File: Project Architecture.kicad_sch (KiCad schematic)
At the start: 0 parts

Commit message: SCH[Power & Balance]: Inital Schamtic for two pages.
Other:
- removed sheet Section A - Title A
- removed sheet Section B - Title B
- added sheet Cell Sense & Balance (cell_sense_and_balance.kicad_sch)
- added sheet Connectors (connectors.kicad_sch)
- added sheet Daisy Chain (daisy_chain.kicad_sch)
- added sheet Mechanical (mechanical.kicad_sch)
- added sheet Power & Reference (power_and_reference.kicad_sch)
- added sheet Temperature Sense (temperature_sense.kicad_sch)
- note removed: "Page 5"

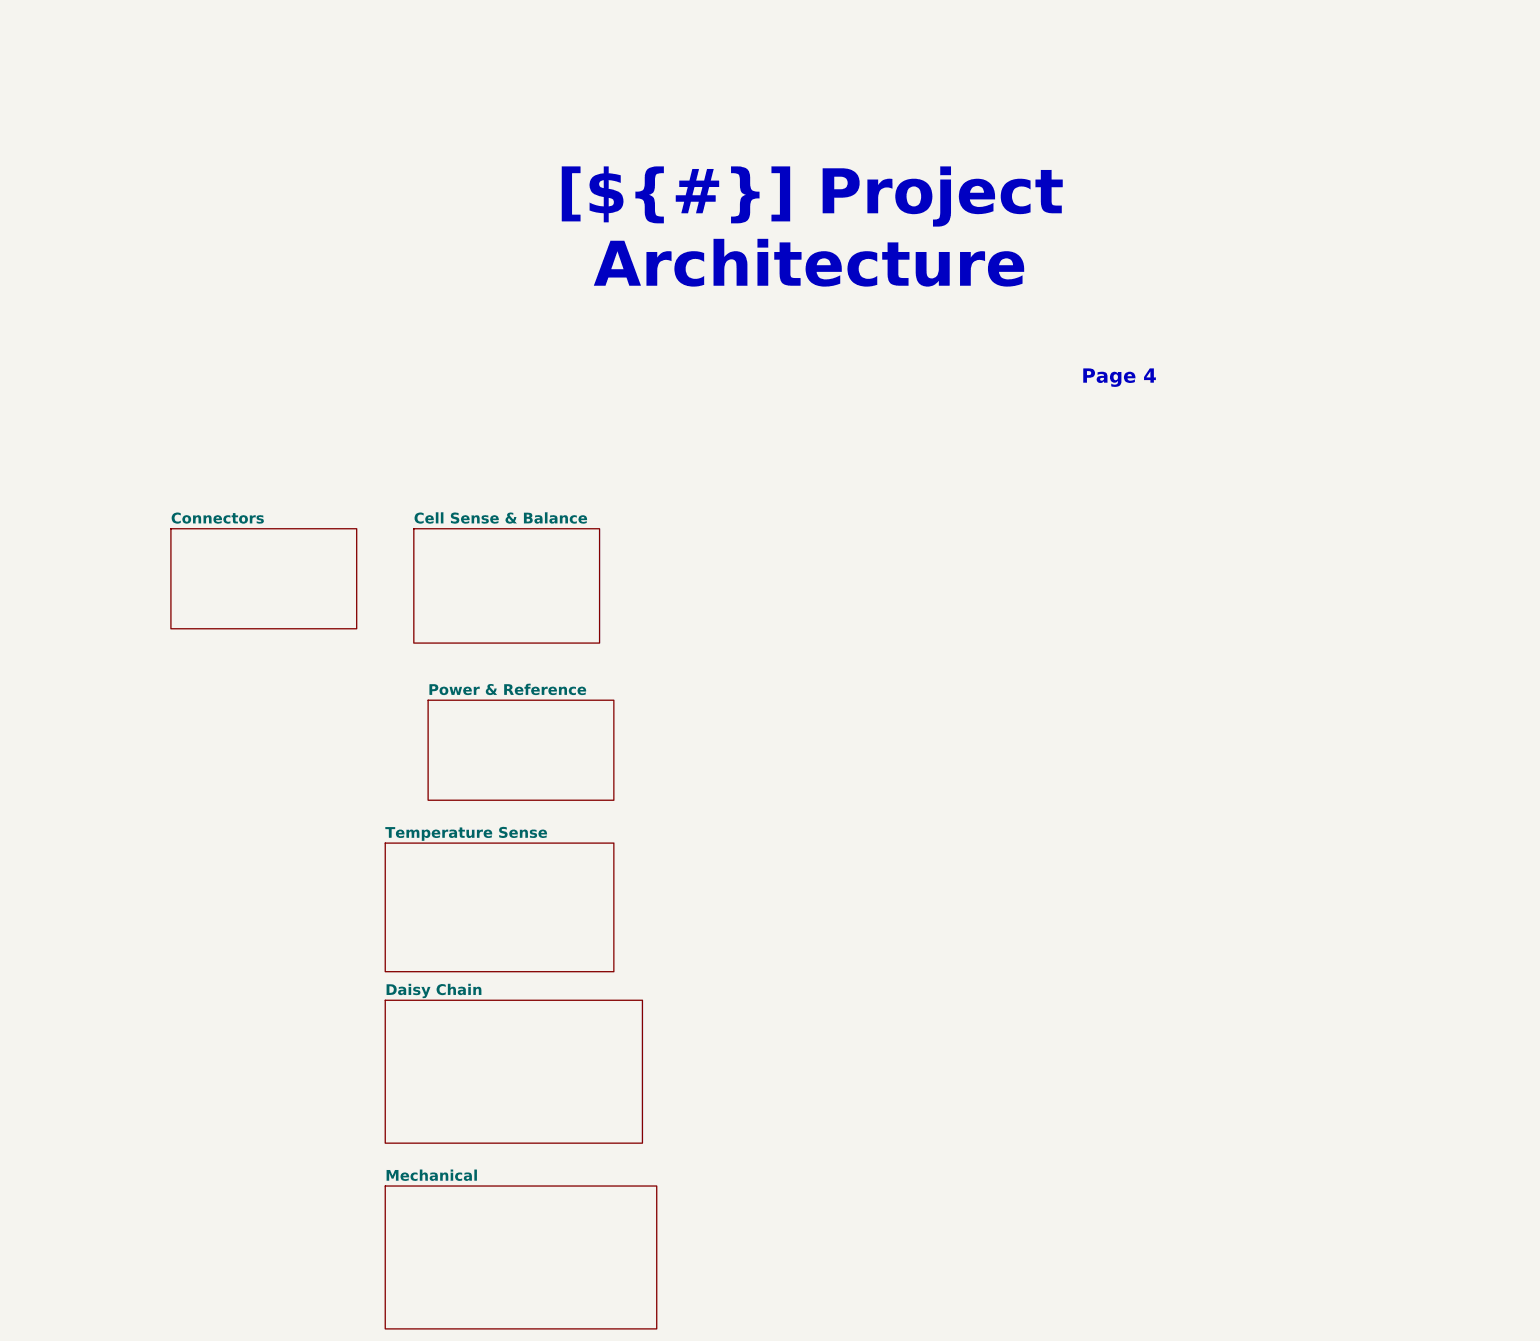
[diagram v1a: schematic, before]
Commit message: SCH:[Hiarchy, Temp, Power]:Inital schmatics of temp, balance, power mostly there need to add design notes and layout notes.
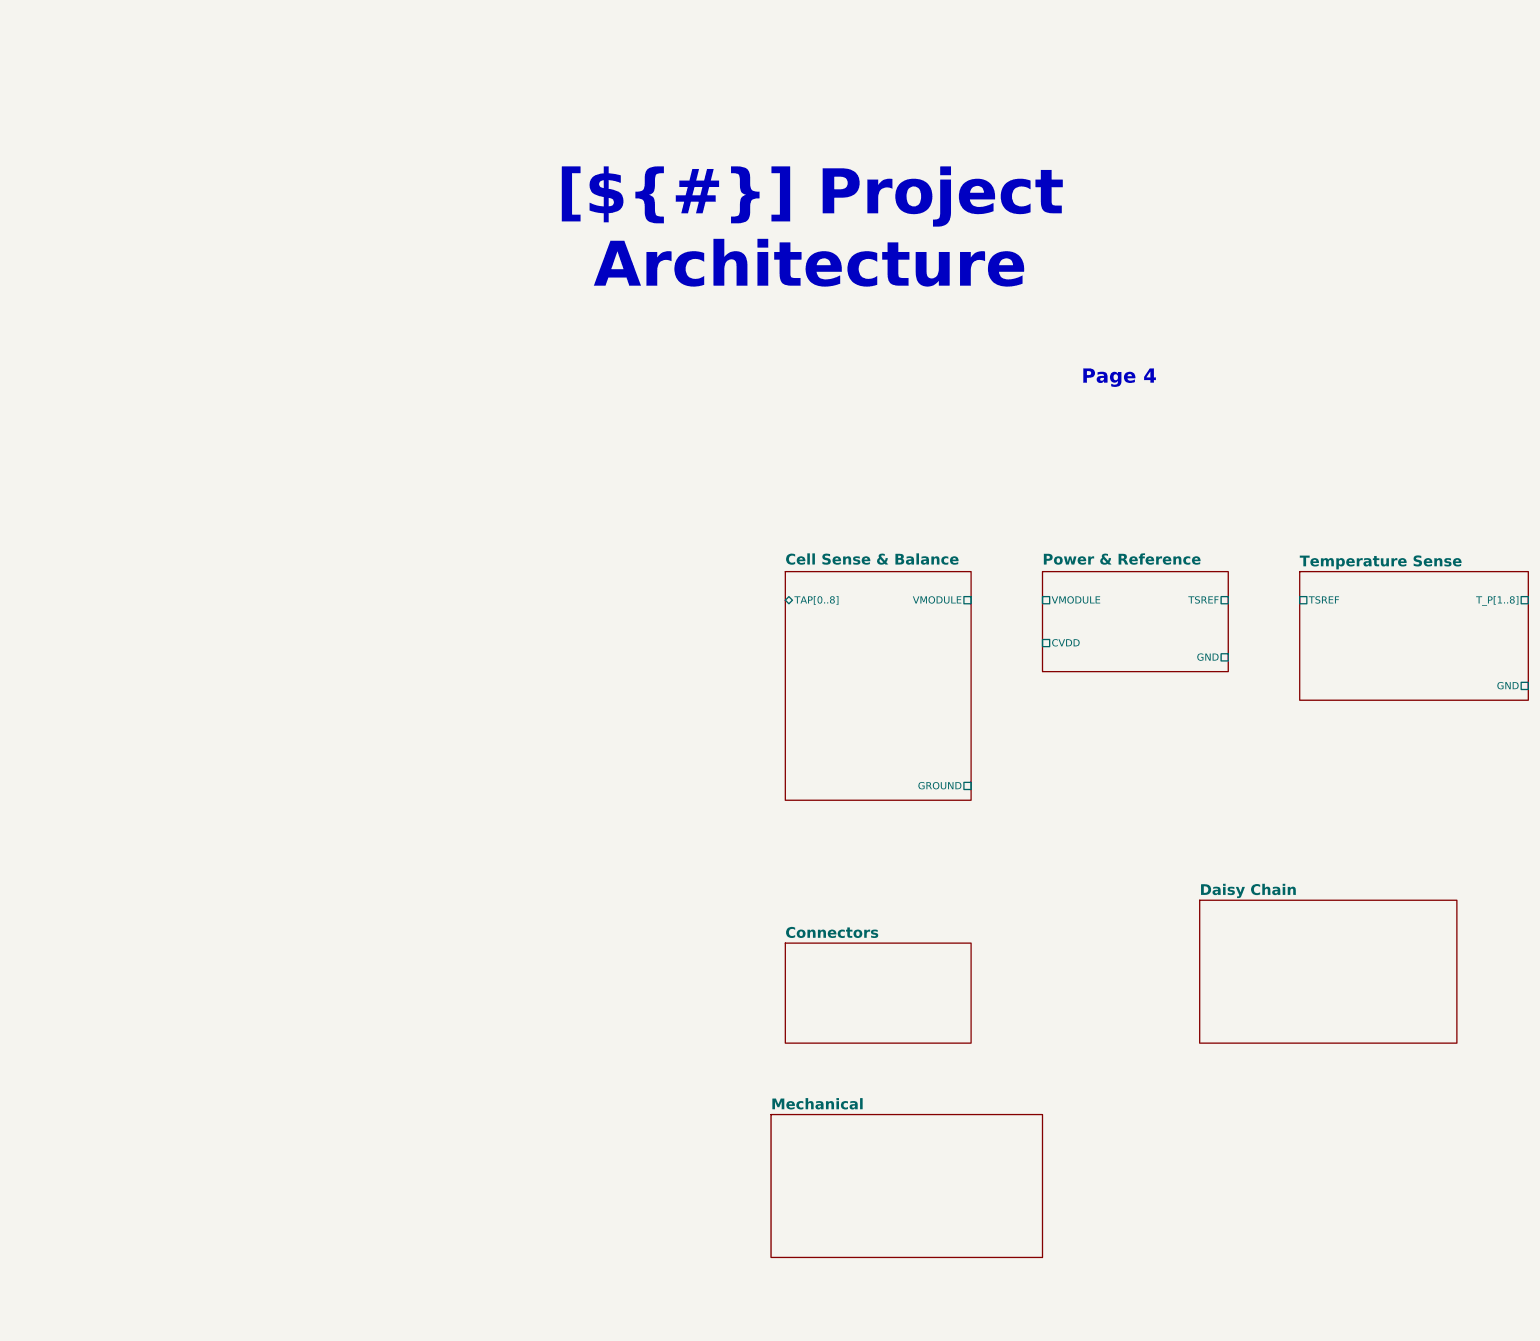
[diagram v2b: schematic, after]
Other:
- sheet Cell Sense & Balance ports: added GROUND, TAP[0..8], VMODULE; removed none
- sheet Power & Reference ports: added CVDD, GND, TSREF, VMODULE; removed none
- sheet Temperature Sense ports: added GND, TSREF, T_P[1..8]; removed none
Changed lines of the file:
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@@
 	)
 	(sheet
-		(at 134.62 137.16)
+		(at 297.18 88.9)
 		(size 40.64 22.86)
 		(exclude_from_sim no)
@@
 		)
 		(property "Sheetname" "Temperature Sense"
-			(at 134.62 136.4484 0)
+			(at 297.18 88.1884 0)
 			(show_name no)
 			(do_not_autoplace no)
@@
 		)
 		(property "Sheetfile" "temperature_sense.kicad_sch"
-			(at 134.62 160.6046 0)
-			(hide yes)
-			(show_name no)
-			(do_not_autoplace no)
-			(effects
-				(font
-					(size 1.27 1.27)
-				)
-				(justify left top)
+			(at 297.18 112.3446 0)
+			(hide yes)
+			(show_name no)
+			(do_not_autoplace no)
+			(effects
+				(font
+					(size 1.27 1.27)
+				)
+				(justify left top)
+			)
+		)
+		(pin "GND" passive
+			(at 337.82 109.22 0)
+			(effects
+				(font
+					(size 1.27 1.27)
+				)
+				(justify right)
+			)
+		)
+		(pin "TSREF" passive
+			(at 297.18 93.98 180)
+			(effects
+				(font
+					(size 1.27 1.27)
+				)
+				(justify left)
+			)
+		)
+		(pin "T_P[1..8]" passive
+			(at 337.82 93.98 0)
+			(effects
+				(font
+					(size 1.27 1.27)
+				)
+				(justify right)
 			)
 		)
@@
 	)
 	(sheet
-		(at 96.52 81.28)
+		(at 205.74 154.94)
 		(size 33.02 17.78)
 		(exclude_from_sim no)
@@
 		)
 		(property "Sheetname" "Connectors"
-			(at 96.52 80.5684 0)
+			(at 205.74 154.2284 0)
 			(show_name no)
 			(do_not_autoplace no)
@@
 		)
 		(property "Sheetfile" "connectors.kicad_sch"
-			(at 96.52 99.6446 0)
+			(at 205.74 173.3046 0)
 			(hide yes)
 			(show_name no)
@@
 	)
 	(sheet
-		(at 142.24 111.76)
+		(at 251.46 88.9)
 		(size 33.02 17.78)
 		(exclude_from_sim no)
@@
 		)
 		(property "Sheetname" "Power & Reference"
-			(at 142.24 111.0484 0)
+			(at 251.46 87.8709 0)
 			(show_name no)
 			(do_not_autoplace no)
@@
 		)
 		(property "Sheetfile" "power_and_reference.kicad_sch"
-			(at 142.24 130.1246 0)
-			(hide yes)
-			(show_name no)
-			(do_not_autoplace no)
-			(effects
-				(font
-					(size 1.27 1.27)
-				)
-				(justify left top)
+			(at 251.46 107.2646 0)
+			(hide yes)
+			(show_name no)
+			(do_not_autoplace no)
+			(effects
+				(font
+					(size 1.27 1.27)
+				)
+				(justify left top)
+			)
+		)
+		(pin "CVDD" passive
+			(at 251.46 101.6 180)
+			(effects
+				(font
+					(size 1.27 1.27)
+				)
+				(justify left)
+			)
+		)
+		(pin "GND" passive
+			(at 284.48 104.14 0)
+			(effects
+				(font
+					(size 1.27 1.27)
+				)
+				(justify right)
+			)
+		)
+		(pin "TSREF" passive
+			(at 284.48 93.98 0)
+			(effects
+				(font
+					(size 1.27 1.27)
+				)
+				(justify right)
+			)
+		)
+		(pin "VMODULE" passive
+			(at 251.46 93.98 180)
+			(effects
+				(font
+					(size 1.27 1.27)
+				)
+				(justify left)
 			)
 		)
@@
 	)
 	(sheet
-		(at 139.7 81.28)
-		(size 33.02 20.32)
+		(at 205.74 88.9)
+		(size 33.02 40.64)
 		(exclude_from_sim no)
 		(in_bom yes)
@@
 		)
 		(property "Sheetname" "Cell Sense & Balance"
-			(at 139.7 80.5684 0)
+			(at 205.74 87.8709 0)
 			(show_name no)
 			(do_not_autoplace no)
@@
 		)
 		(property "Sheetfile" "cell_sense_and_balance.kicad_sch"
-			(at 139.7 102.1846 0)
-			(hide yes)
-			(show_name no)
-			(do_not_autoplace no)
-			(effects
-				(font
-					(size 1.27 1.27)
-				)
-				(justify left top)
+			(at 205.74 130.1246 0)
+			(hide yes)
+			(show_name no)
+			(do_not_autoplace no)
+			(effects
+				(font
+					(size 1.27 1.27)
+				)
+				(justify left top)
+			)
+		)
+		(pin "GROUND" passive
+			(at 238.76 127 0)
+			(effects
+				(font
+					(size 1.27 1.27)
+				)
+				(justify right)
+			)
+		)
+		(pin "TAP[0..8]" bidirectional
+			(at 205.74 93.98 180)
+			(effects
+				(font
+					(size 1.27 1.27)
+				)
+				(justify left)
+			)
+		)
+		(pin "VMODULE" passive
+			(at 238.76 93.98 0)
+			(effects
+				(font
+					(size 1.27 1.27)
+				)
+				(justify right)
 			)
 		)
@@
 	)
 	(sheet
-		(at 134.62 165.1)
+		(at 279.4 147.32)
 		(size 45.72 25.4)
 		(exclude_from_sim no)
@@
 		)
 		(property "Sheetname" "Daisy Chain"
-			(at 134.62 164.3884 0)
+			(at 279.4 146.6084 0)
 			(show_name no)
 			(do_not_autoplace no)
@@
 		)
 		(property "Sheetfile" "daisy_chain.kicad_sch"
-			(at 134.62 191.0846 0)
+			(at 279.4 173.3046 0)
 			(hide yes)
 			(show_name no)
@@
 	)
 	(sheet
-		(at 134.62 198.12)
+		(at 203.2 185.42)
 		(size 48.26 25.4)
 		(exclude_from_sim no)
@@
 		)
 		(property "Sheetname" "Mechanical"
-			(at 134.62 197.4084 0)
+			(at 203.2 184.7084 0)
 			(show_name no)
 			(do_not_autoplace no)
@@
 		)
 		(property "Sheetfile" "mechanical.kicad_sch"
-			(at 134.62 224.1046 0)
-			(hide yes)
-			(show_name no)
+			(at 203.2 211.4046 0)
+			(hide yes)
+			(show_name no)

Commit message: SCH: Schmatic is close to final, need to resolve a few ERC errors nothing major. Largest change will be adding seporate wires for VBAT and RefGround / Tap 0. connector position and types may change as mechaincal posision/layout is finalaized as well so holding off on layout for now.
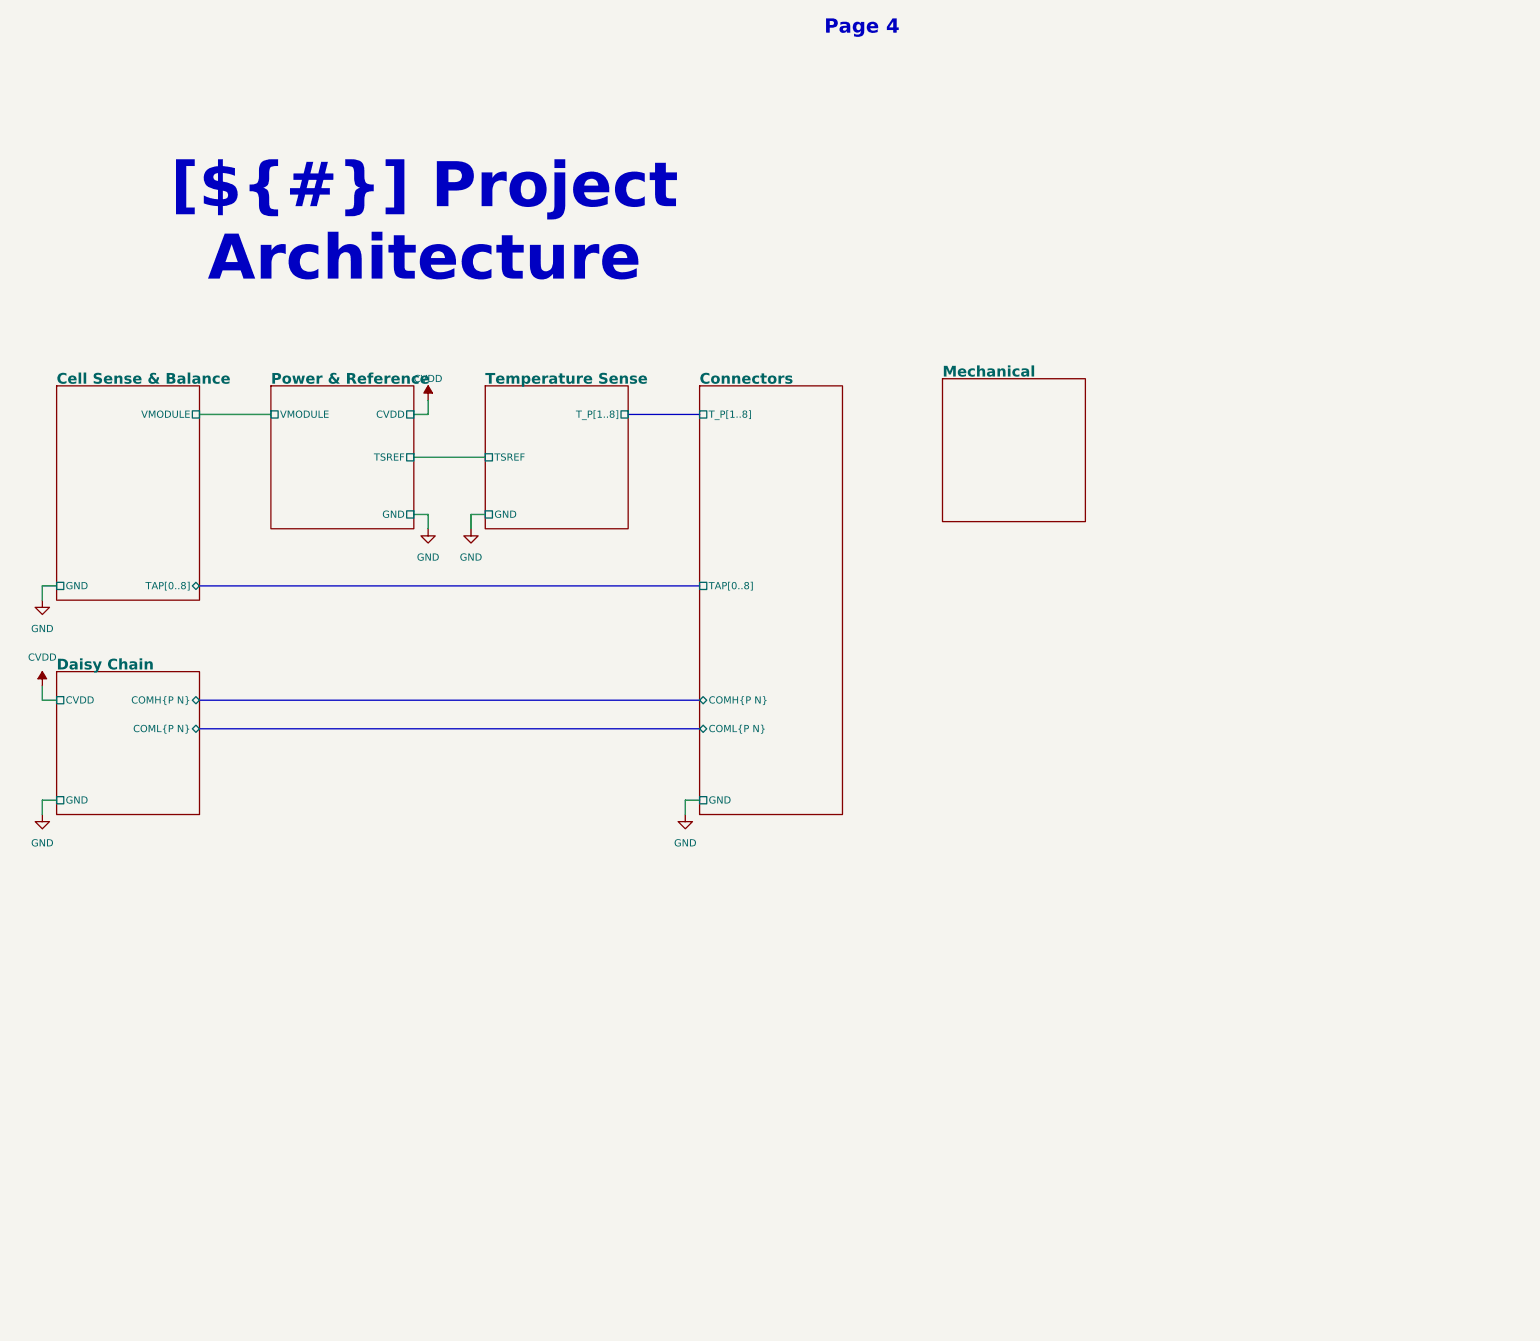
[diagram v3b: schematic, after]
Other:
- sheet Cell Sense & Balance ports: added GND; removed GROUND
- sheet Connectors ports: added COMH{P N}, COML{P N}, GND, TAP[0..8], T_P[1..8]; removed none
- sheet Daisy Chain ports: added COMH{P N}, COML{P N}, CVDD, GND; removed none
